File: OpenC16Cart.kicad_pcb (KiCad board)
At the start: 2 copper layers, 52 x 65 mm, 16 parts, among them J1 CONN_02X03, J11 CONN_01X03, J12 CONN_01X03, J2 CONN_01X03, J21 CONN_01X03, J22 CONN_01X03, J3 CONN_01X03, J4 CONN_02X03, J5 CONN_01X03, J6 CONN_01X03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

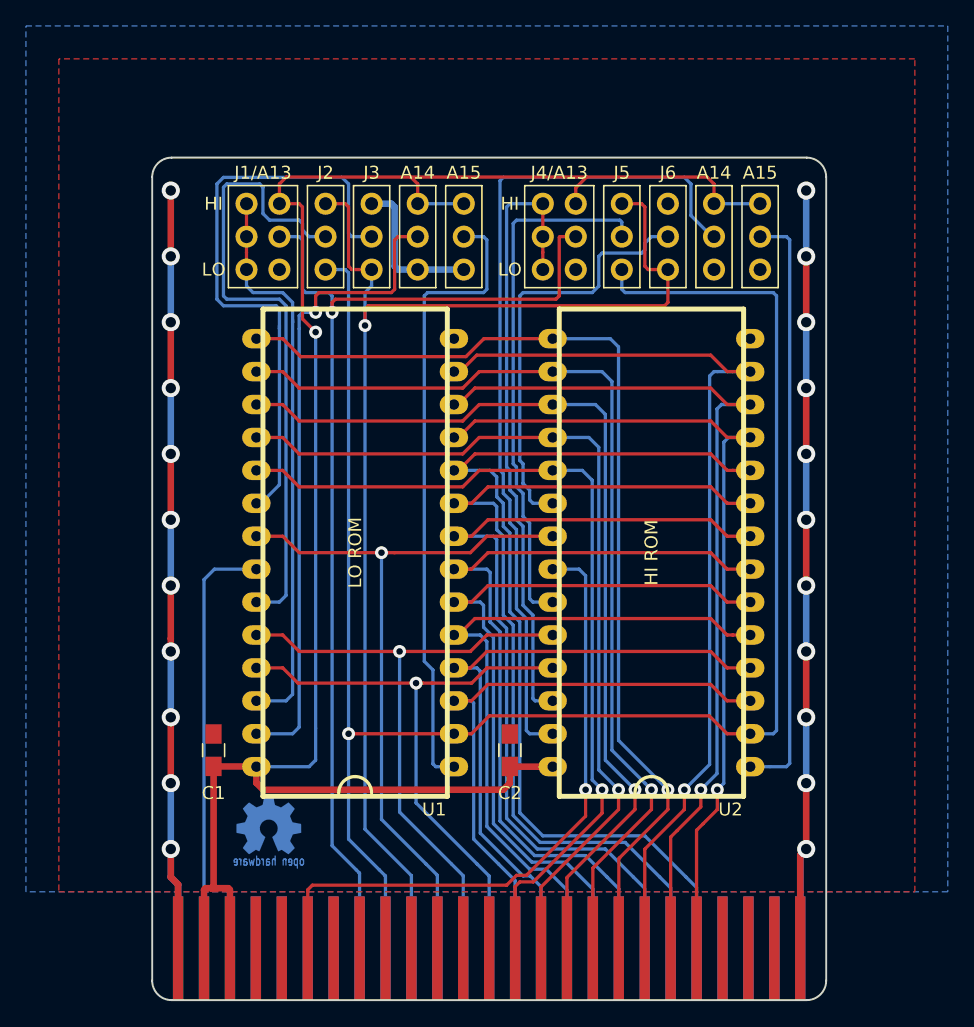
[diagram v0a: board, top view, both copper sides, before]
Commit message: Layout redone, schematics simplified
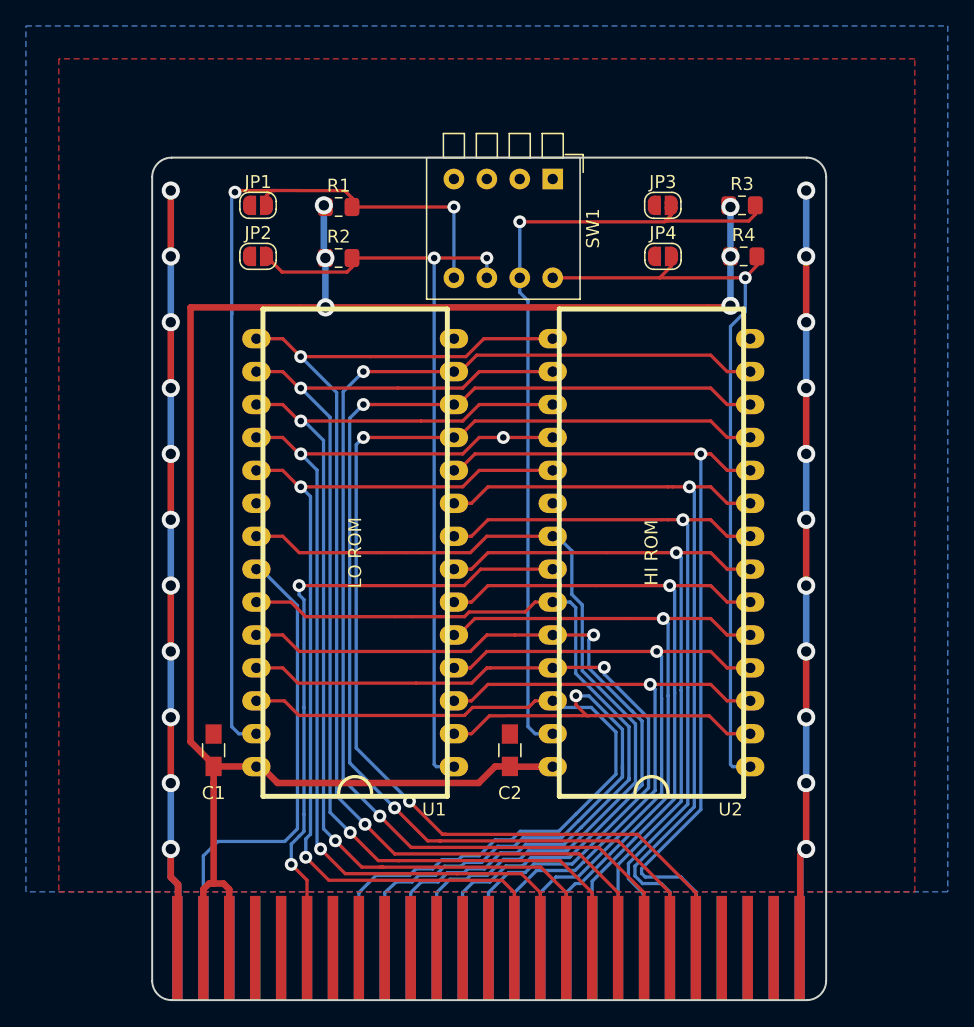
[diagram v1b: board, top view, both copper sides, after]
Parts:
- removed G***: LOGO, w_logo:Logo_copper_OSHW_6x6mm
- removed J1, J4: CONN_02X03, OpenC16Cart:Pin_Header_Straight_2x03-ModSilkS
- removed J11, J12, J2, J21, J22, J3, J6: CONN_01X03, OpenC16Cart:Pin_Header_Straight_1x03-ModSilkS
- removed J7: C16-Exp-Port, OpenC16Cart:C16_Cart_Conn
- added JP1: U1 A14/~PGM, Jumper:SolderJumper-2_P1.3mm_Open_RoundedPad1.0x1.5mm, F.Cu at (129.7, 67.2)
- added JP2: U1 A15/VPP, Jumper:SolderJumper-2_P1.3mm_Open_RoundedPad1.0x1.5mm, F.Cu at (129.7, 71.1)
- added JP3: U2 A14/~PGM, Jumper:SolderJumper-2_P1.3mm_Open_RoundedPad1.0x1.5mm, F.Cu at (160.9, 67.2)
- added JP4: U2 A15/VPP, Jumper:SolderJumper-2_P1.3mm_Open_RoundedPad1.0x1.5mm, F.Cu at (160.9, 71.1)
- added R1: 10kΩ, Resistor_SMD:R_0805_2012Metric_Pad1.15x1.40mm_HandSolder, F.Cu at (135.9, 67.3)
- added R2: 10kΩ, Resistor_SMD:R_0805_2012Metric_Pad1.15x1.40mm_HandSolder, F.Cu at (135.9, 71.2)
- added R3: 10kΩ, Resistor_SMD:R_0805_2012Metric_Pad1.15x1.40mm_HandSolder, F.Cu at (167.0, 67.2)
- added R4: 10kΩ, Resistor_SMD:R_0805_2012Metric_Pad1.15x1.40mm_HandSolder, F.Cu at (167.1, 71.1)
- added SW1: SW_DIP_x04, Button_Switch_THT:SW_DIP_SPSTx04_Piano_10.8x11.72mm_W7.62mm_P2.54mm, F.Cu at (152.4, 65.2)
- J5: value CONN_01X03 -> C16-Exp-Port; footprint OpenC16Cart:Pin_Header_Straight_1x03-ModSilkS -> OpenC16Cart:C16_Cart_Conn
- U1: value 27512 - LO ROM -> LO ROM
- U2: value 27512 - HI ROM -> HI ROM
- moved J5 58.3 mm to (147.4, 124.5)
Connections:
- J5 pad 1: /a11_conn -> GND
- J5 pad 2: /a11_u2 -> VCC
- J5 pad 3: /a12 -> VCC
- U1 pad 1: /a15_u1 -> U1-A15
- U1 pad 20: //ce_u1 -> GND
- U1 pad 22: Net-(J7-PadB) -> Net-(J5-PadB)
- U1 pad 23: /a11_u1 -> /a11
- U1 pad 26: /a13_u1 -> /a13
- U1 pad 27: /a14_u1 -> U1-A14
- U2 pad 1: /a15_u2 -> U2-A15
- U2 pad 20: //ce_u2 -> GND
- U2 pad 22: Net-(J7-Pad6) -> Net-(J5-Pad6)
- U2 pad 23: /a11_u2 -> /a11
- U2 pad 26: /a13_u2 -> /a13
- U2 pad 27: /a14_u2 -> U2-A14
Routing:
- net /a11_conn: track 98.1 -> 0.00 mm, vias 1 -> 0
- net /a13_conn: track 83.7 -> 0.00 mm, vias 1 -> 0
- net /a12: track 136.6 -> 62.7 mm
- net U1-A14: track 0.00 -> 68.7 mm, vias 0 -> 2
- net /a11: track 0.00 -> 65.5 mm
- net /a14_u2: track 65.3 -> 0.00 mm
- net U2-A14: track 0.00 -> 61.8 mm, vias 0 -> 1
- net /a13: track 0.00 -> 60.8 mm
- net U1-A15: track 0.00 -> 60.6 mm, vias 0 -> 2
- net U2-A15: track 0.00 -> 58.5 mm, vias 0 -> 1
- net /a14_u1: track 49.9 -> 0.00 mm, vias 1 -> 0
- net Net-(J7-Pad6): track 49.6 -> 0.00 mm, vias 1 -> 0
- net /a11_u1: track 49.5 -> 0.00 mm
- net Net-(J5-Pad6): track 0.00 -> 49.1 mm, vias 0 -> 2
- net /a15_u1: track 48.8 -> 0.00 mm
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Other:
- rule trace_min: 0.1524 -> 0.127
- board text added: "27128 Populate R1/R3 (10kΩ) 27256 SW1/3 selects"
- board text added: "27512 Populate R1-R4 (10kΩ) SW1-4 selects"
- board text added: "Commodore C16 + Plus/4 ROM Cartridge"
- board text added: "JP1/R1/SW1-4 U1 Pin 27 (A14) JP2/R2/SW1-3 U1 Pin 1 (A15) JP3/R3/SW1-2 U2 Pin 27 (A14) JP4/R4/SW1-1 U2 Pin 1 (A15)"
- board text added: "U1: Lower ROM U2: Upper ROM"
- board text added: "https://github.com/hanshuebner/OpenC16Cart"
- board text removed: "A14"
- board text removed: "A15"
- board text removed: "HI"
- board text removed: "J1/A13"
- board text removed: "J4/A13"
- board text removed: "LO"
- board text removed: "V3"
- board text removed: "github.com/SukkoPera/OpenC16Cart"

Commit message: Generate production gerbers
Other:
- board text added: "Version 1 12. Juli 2020"
